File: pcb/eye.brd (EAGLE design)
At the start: 158.8 x 54 mm, 92 parts, among them J2 JST-ZH-5SMD-RA, U1 WS2812, U10 WS2812, U11 WS2812, U12 WS2812, U13 WS2812, U14 WS2812, U15 WS2812, U16 WS2812, U17 WS2812, U18 WS2812, U19 WS2812, U2 WS2812, U20 WS2812, U21 WS2812, U22 WS2812, U23 WS2812, U24 WS2812, U25 WS2812, U26 WS2812, U27 WS2812, U28 WS2812, U29 WS2812, U3 WS2812, U30 WS2812, U31 WS2812, U32 WS2812, U33 WS2812, U34 WS2812, U35 WS2812, U36 WS2812, U37 WS2812, U38 WS2812, U39 WS2812, U4 WS2812, U40 WS2812, U41 WS2812, U42 WS2812, U43 WS2812, U44 WS2812, U45 WS2812, U46 WS2812, U47 WS2812, U48 WS2812, U49 WS2812, U5 WS2812, U50 WS2812, U51 WS2812, U52 WS2812, U53 WS2812, U54 WS2812, U55 WS2812, U56 WS2812, U57 WS2812, U58 WS2812, U59 WS2812, U6 WS2812, U60 WS2812, U61 32U4, U7 WS2812, U8 WS2812, U9 WS2812, X1 ECS-160-20-3X-TR

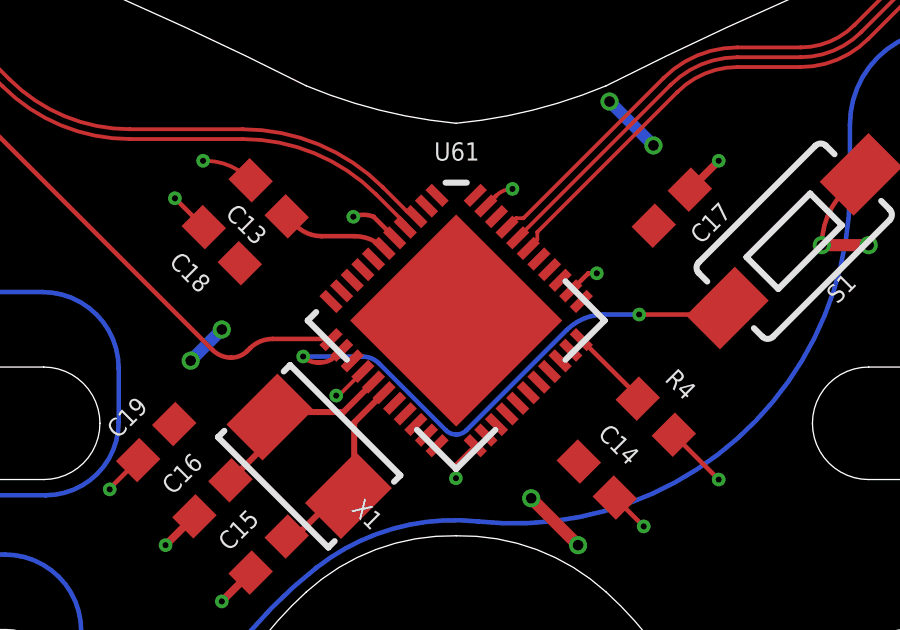
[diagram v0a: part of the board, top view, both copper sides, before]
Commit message: connect MCU grounds under EP
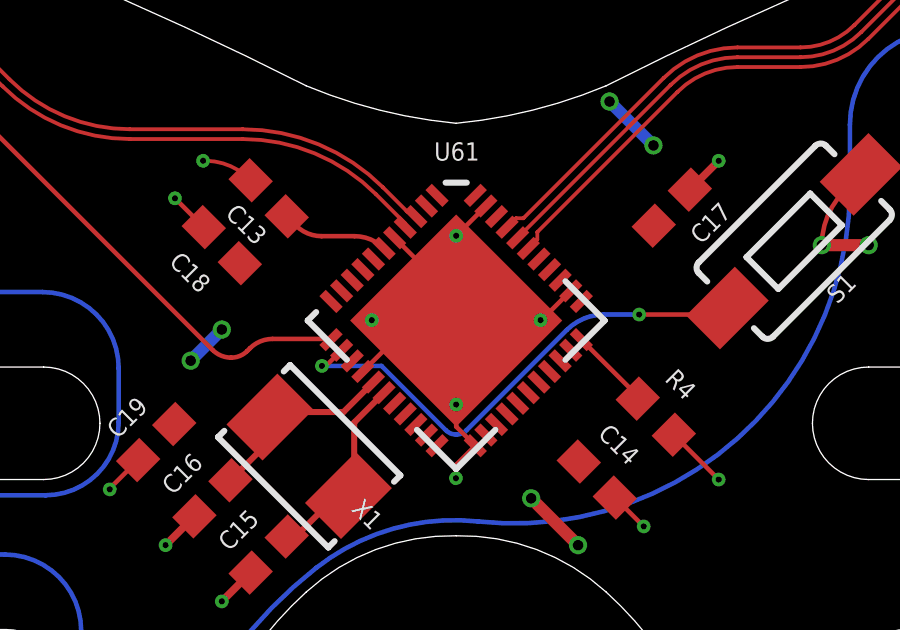
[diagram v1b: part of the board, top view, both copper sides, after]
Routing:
- net GND: track 223.1 -> 227.4 mm
- net RST: track 18.1 -> 17.1 mm
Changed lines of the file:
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@@
 <wire x1="10.5" y1="49.7" x2="10.1" y2="49.7" width="0.1524" layer="41"/>
 <wire x1="10.1" y1="49.7" x2="10.1" y2="50.9" width="0.1524" layer="41"/>
-<wire x1="76.2" y1="42.8" x2="80" y2="39" width="0.1524" layer="41"/>
-<wire x1="80" y1="39" x2="83.8" y2="42.8" width="0.1524" layer="41"/>
-<wire x1="83.8" y1="42.8" x2="80" y2="46.6" width="0.1524" layer="41"/>
-<wire x1="80" y1="46.6" x2="76.2" y2="42.8" width="0.1524" layer="41"/>
+<wire x1="77.6" y1="41.3" x2="80" y2="38.9" width="0.1524" layer="41"/>
+<wire x1="80.3" y1="39.3" x2="83.8" y2="42.8" width="0.1524" layer="41"/>
+<wire x1="83.8" y1="42.8" x2="83.5" y2="43.1" width="0.1524" layer="41"/>
+<wire x1="83.2" y1="43.5" x2="80.7" y2="46" width="0.1524" layer="41"/>
+<wire x1="80.3" y1="46.3" x2="80" y2="46.6" width="0.1524" layer="41"/>
+<wire x1="80" y1="46.6" x2="78.7" y2="45.3" width="0.1524" layer="41"/>
+<wire x1="78.2" y1="44.8" x2="76.2" y2="42.8" width="0.1524" layer="41"/>
+<wire x1="76.2" y1="42.8" x2="76.2" y2="42.7" width="0.1524" layer="41"/>
+<wire x1="76.2" y1="42.7" x2="77.2" y2="41.7" width="0.1524" layer="41"/>
 </plain>
 <attributes>
@@
 <wire x1="73.14895625" y1="34.39895625" x2="72.1875" y2="33.4375" width="0.254" layer="1"/>
 <via x="72.1875" y="33.4375" extent="1-16" drill="0.2"/>
-<wire x1="77.9493875" y1="45.557715625" x2="77.248340625" y2="46.2587625" width="0.1524" layer="1"/>
-<wire x1="77.248340625" y1="46.2587625" x2="76.5712625" y2="46.2587625" width="0.1524" layer="1" curve="45"/>
-<via x="76.5712625" y="46.2587625" extent="1-16" drill="0.2"/>
 <wire x1="73.14895625" y1="47.476040625" x2="71.682228125" y2="48.125" width="0.127" layer="1" curve="45"/>
 <wire x1="71.682228125" y1="48.125" x2="71.5625" y2="48.125" width="0.127" layer="1"/>
 <via x="71.5625" y="48.125" extent="1-16" drill="0.2"/>
-<wire x1="80.989946875" y1="46.618375" x2="81.335684375" y2="46.9641125" width="0.1524" layer="1"/>
-<wire x1="81.335684375" y1="46.9641125" x2="81.875" y2="47.1875" width="0.127" layer="1" curve="-45"/>
-<via x="81.875" y="47.1875" extent="1-16" drill="0.2"/>
-<wire x1="84.6875" y1="44.375" x2="84.403428125" y2="44.375" width="0.1524" layer="1"/>
-<wire x1="84.403428125" y1="44.375" x2="83.818375" y2="43.789946875" width="0.1524" layer="1"/>
-<via x="84.6875" y="44.375" extent="1-16" drill="0.2"/>
-<wire x1="76.888728125" y1="41.102940625" x2="76.042775" y2="40.2569875" width="0.127" layer="1"/>
-<wire x1="76.00138125" y1="40.29838125" x2="76.042775" y2="40.2569875" width="0.127" layer="1"/>
-<via x="76.00138125" y="40.29838125" extent="1-16" drill="0.2"/>
 <via x="88.75" y="48.125" extent="1-16" drill="0.2"/>
 <wire x1="141.15" y1="54.2" x2="141.947896875" y2="54.2" width="0.1524" layer="1"/>
@@
 <wire x1="93.4948" y1="47.671578125" x2="92.93121875" y2="47.107996875" width="0.1524" layer="1"/>
 <wire x1="92.93121875" y1="47.107996875" x2="92.1875" y2="45.3125" width="0.1524" layer="1" curve="45"/>
+<via x="80" y="45.625" extent="1-16" drill="0.2"/>
+<via x="82.8125" y="42.8125" extent="1-16" drill="0.2"/>
+<via x="77.1875" y="42.8125" extent="1-16" drill="0.2"/>
+<via x="80" y="40" extent="1-16" drill="0.2"/>
+<wire x1="76.888728125" y1="41.102940625" x2="77.6607875" y2="41.875" width="0.1524" layer="1"/>
+<wire x1="80.63639375" y1="38.62806875" x2="80" y2="39.2644625" width="0.1524" layer="1"/>
+<wire x1="80" y1="39.2644625" x2="80" y2="40" width="0.1524" layer="1"/>
+<wire x1="77.9493875" y1="45.557715625" x2="78.75" y2="44.757103125" width="0.1524" layer="1"/>
+<wire x1="80.989946875" y1="46.618375" x2="80.989946875" y2="46.614946875" width="0.1524" layer="1"/>
+<wire x1="80.989946875" y1="46.614946875" x2="80" y2="45.625" width="0.1524" layer="1"/>
+<wire x1="83.818375" y1="43.789946875" x2="82.840928125" y2="42.8125" width="0.1524" layer="1"/>
+<wire x1="82.840928125" y1="42.8125" x2="82.8125" y2="42.8125" width="0.1524" layer="1"/>
+<wire x1="77.1875" y1="42.8125" x2="77.6607875" y2="42.3392125" width="0.1524" layer="1"/>
+<wire x1="77.6607875" y1="42.3392125" x2="77.6607875" y2="41.875" width="0.1524" layer="1"/>
+<wire x1="78.75" y1="44.757103125" x2="79.132103125" y2="44.757103125" width="0.1524" layer="1"/>
+<wire x1="79.132103125" y1="44.757103125" x2="80" y2="45.625" width="0.1524" layer="1"/>
 </signal>
 <signal name="N$6">
@@
 <contactref element="U61" pad="13"/>
 <contactref element="S1" pad="2"/>
-<via x="74.9" y="41.6" extent="1-16" drill="0.2"/>
-<wire x1="74.9" y1="41.6" x2="76.872159375" y2="41.6" width="0.1524" layer="16"/>
-<wire x1="76.872159375" y1="41.6" x2="77.43181875" y2="41.36818125" width="0.1524" layer="16" curve="-45"/>
+<via x="75.525" y="41.2875" extent="1-16" drill="0.2"/>
+<wire x1="75.525" y1="41.2875" x2="77.5125" y2="41.2875" width="0.1524" layer="16"/>
 <wire x1="79.658578125" y1="39.141421875" x2="80" y2="39" width="0.1524" layer="16" curve="45"/>
 <wire x1="80" y1="39" x2="80.341421875" y2="39.141421875" width="0.1524" layer="16" curve="45"/>
@@
 <wire x1="86.1" y1="43" x2="88.278428125" y2="43" width="0.1524" layer="1"/>
 <wire x1="88.278428125" y1="43" x2="89.040028125" y2="43.21680625" width="0.1524" layer="1" curve="45"/>
-<wire x1="77.43181875" y1="41.36818125" x2="79.658578125" y2="39.141421875" width="0.1524" layer="16"/>
+<wire x1="77.5125" y1="41.2875" x2="79.658578125" y2="39.141421875" width="0.1524" layer="16"/>
 <wire x1="80.341421875" y1="39.141421875" x2="83.685340625" y2="42.485340625" width="0.1524" layer="16"/>
 <wire x1="76.181621875" y1="41.81005" x2="75.992890625" y2="41.62131875" width="0.1524" layer="1"/>
-<wire x1="75.992890625" y1="41.62131875" x2="75.458578125" y2="41.4" width="0.1524" layer="1" curve="-45"/>
-<wire x1="75.458578125" y1="41.4" x2="75.38284375" y2="41.4" width="0.1524" layer="1"/>
-<wire x1="75.38284375" y1="41.4" x2="74.9" y2="41.6" width="0.1524" layer="1" curve="-45"/>
+<wire x1="76.181621875" y1="41.81005" x2="75.659071875" y2="41.2875" width="0.1524" layer="1"/>
+<wire x1="75.659071875" y1="41.2875" x2="75.525" y2="41.2875" width="0.1524" layer="1"/>
 </signal>
 <signal name="N$77">

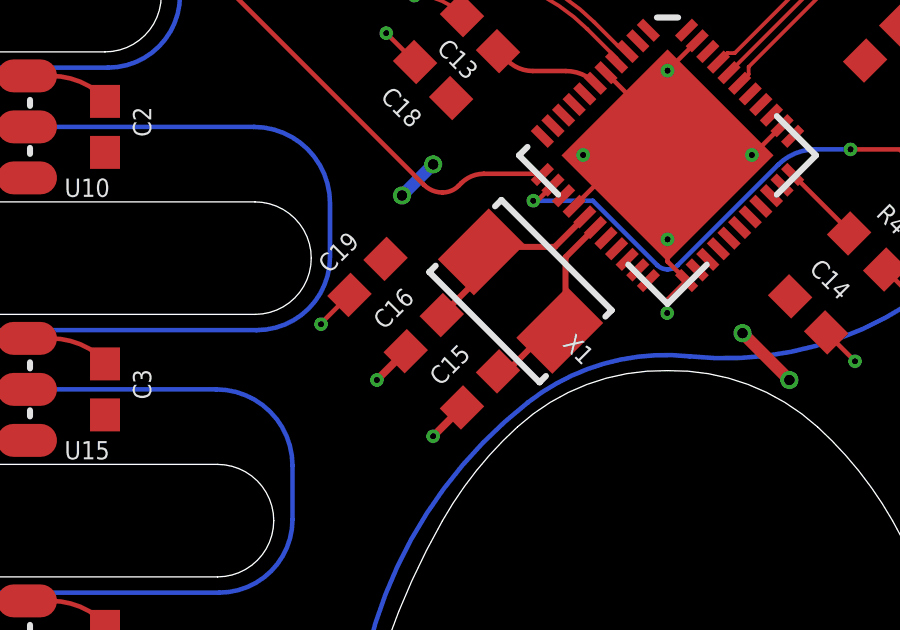
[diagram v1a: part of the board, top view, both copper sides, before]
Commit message: fix X1 silkscreen and caps
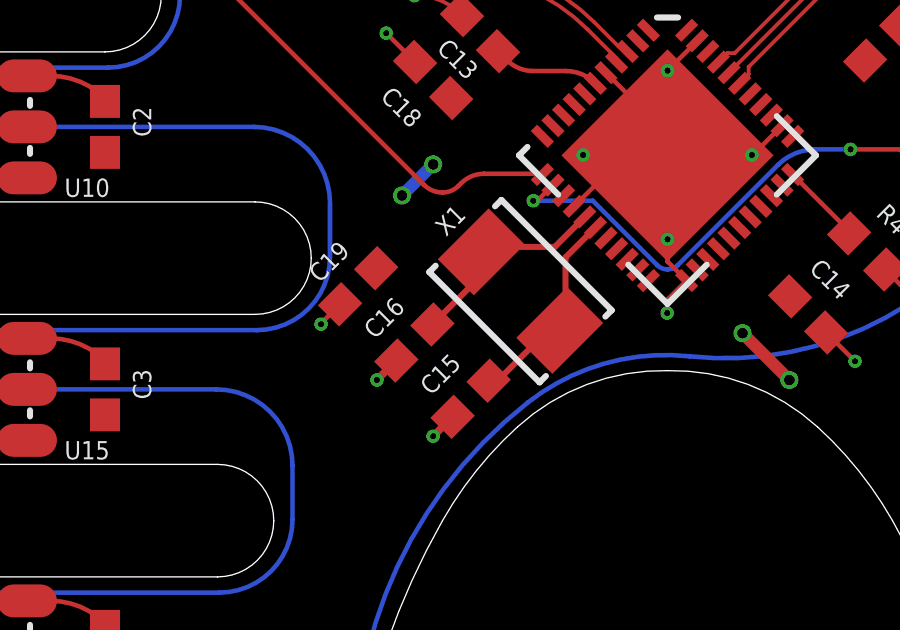
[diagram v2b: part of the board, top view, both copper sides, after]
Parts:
- moved C15 0.44 mm to (73.4, 34.7)
- moved C16 0.44 mm to (71.6, 36.6)
- moved C19 0.44 mm to (69.7, 38.4)
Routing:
- net GND: track 227.4 -> 226.1 mm
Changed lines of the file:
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@@
 <setting verticaltext="up"/>
 </settings>
-<grid distance="0.1" unitdist="mm" unit="mm" style="lines" multiple="1" display="yes" altdistance="5" altunitdist="mil" altunit="mil"/>
+<grid distance="0.3125" unitdist="mm" unit="mm" style="lines" multiple="1" display="yes" altdistance="5" altunitdist="mil" altunit="mil"/>
 <layers>
 <layer number="1" name="Top" color="4" fill="1" visible="yes" active="yes"/>
@@
 </element>
 <element name="X1" library="SparkFun-Clocks" package="CRYSTAL-SMD-5X3.2-2PAD" value="ECS-160-20-3X-TR" x="75.1" y="38.275" smashed="yes" rot="R315">
-<attribute name="NAME" x="76.47204375" y="36.479271875" size="0.6096" layer="25" ratio="10" rot="R315"/>
+<attribute name="NAME" x="72.620728125" y="40.07204375" size="0.6096" layer="25" ratio="10" rot="R45"/>
 <attribute name="VALUE" x="68.095403125" y="39.35263125" size="1.27" layer="27" ratio="10" rot="R315"/>
 </element>
-<element name="C15" library="rcl" library_urn="urn:adsk.eagle:library:334" package="C0603" package3d_urn="urn:adsk.eagle:package:23616/2" value="20p" x="73.75" y="35" smashed="yes" rot="R225">
-<attribute name="NAME" x="73.046046875" y="36.562496875" size="0.6096" layer="25" rot="R225"/>
-<attribute name="POPULARITY" value="73" x="75.959703125" y="78.75223125" size="1.778" layer="27" font="vector" rot="R225" display="off"/>
-<attribute name="SPICEPREFIX" value="C" x="75.959703125" y="78.75223125" size="1.778" layer="27" font="vector" rot="R225" display="off"/>
-<attribute name="VALUE" x="72.851971875" y="37.694071875" size="1.27" layer="27" rot="R225"/>
-</element>
-<element name="C16" library="rcl" library_urn="urn:adsk.eagle:library:334" package="C0603" package3d_urn="urn:adsk.eagle:package:23616/2" value="20p" x="71.875" y="36.875" smashed="yes" rot="R225">
-<attribute name="NAME" x="71.171053125" y="38.437496875" size="0.6096" layer="25" rot="R225"/>
-<attribute name="POPULARITY" value="73" x="73.200828125" y="88.582178125" size="1.778" layer="27" font="vector" rot="R225" display="off"/>
-<attribute name="SPICEPREFIX" value="C" x="73.200828125" y="88.582178125" size="1.778" layer="27" font="vector" rot="R225" display="off"/>
-<attribute name="VALUE" x="70.976971875" y="39.569071875" size="1.27" layer="27" rot="R225"/>
+<element name="C15" library="rcl" library_urn="urn:adsk.eagle:library:334" package="C0603" package3d_urn="urn:adsk.eagle:package:23616/2" value="20p" x="73.4375" y="34.6875" smashed="yes" rot="R225">
+<attribute name="NAME" x="72.733546875" y="36.249996875" size="0.6096" layer="25" rot="R225"/>
+<attribute name="POPULARITY" value="73" x="75.647203125" y="78.43973125" size="1.778" layer="27" font="vector" rot="R225" display="off"/>
+<attribute name="SPICEPREFIX" value="C" x="75.647203125" y="78.43973125" size="1.778" layer="27" font="vector" rot="R225" display="off"/>
+<attribute name="VALUE" x="72.539471875" y="37.381571875" size="1.27" layer="27" rot="R225"/>
+</element>
+<element name="C16" library="rcl" library_urn="urn:adsk.eagle:library:334" package="C0603" package3d_urn="urn:adsk.eagle:package:23616/2" value="20p" x="71.5625" y="36.5625" smashed="yes" rot="R225">
+<attribute name="NAME" x="70.858553125" y="38.124996875" size="0.6096" layer="25" rot="R225"/>
+<attribute name="POPULARITY" value="73" x="72.888328125" y="88.269678125" size="1.778" layer="27" font="vector" rot="R225" display="off"/>
+<attribute name="SPICEPREFIX" value="C" x="72.888328125" y="88.269678125" size="1.778" layer="27" font="vector" rot="R225" display="off"/>
+<attribute name="VALUE" x="70.664471875" y="39.256571875" size="1.27" layer="27" rot="R225"/>
 </element>
 <element name="U61" library="SparkFun-IC-Microcontroller" package="QFN-44" value="32U4" x="80" y="42.8" smashed="yes" rot="R315">
@@
 <attribute name="VALUE" x="73.983553125" y="46.210528125" size="1.27" layer="27" rot="R135"/>
 </element>
-<element name="C19" library="rcl" library_urn="urn:adsk.eagle:library:334" package="C0603" package3d_urn="urn:adsk.eagle:package:23616/2" value="" x="70" y="38.75" smashed="yes" rot="R225">
-<attribute name="NAME" x="69.335525" y="40.3125" size="0.6096" layer="25" rot="R225"/>
-<attribute name="POPULARITY" value="73" x="70" y="38.75" size="1.778" layer="27" rot="R225" display="off"/>
-<attribute name="SPICEPREFIX" value="C" x="70" y="38.75" size="1.778" layer="27" rot="R225" display="off"/>
-<attribute name="VALUE" x="69.101975" y="40.546053125" size="1.27" layer="27" rot="R225"/>
+<element name="C19" library="rcl" library_urn="urn:adsk.eagle:library:334" package="C0603" package3d_urn="urn:adsk.eagle:package:23616/2" value="" x="69.6875" y="38.4375" smashed="yes" rot="R225">
+<attribute name="NAME" x="69.023025" y="40" size="0.6096" layer="25" rot="R225"/>
+<attribute name="POPULARITY" value="73" x="69.6875" y="38.4375" size="1.778" layer="27" rot="R225" display="off"/>
+<attribute name="SPICEPREFIX" value="C" x="69.6875" y="38.4375" size="1.778" layer="27" rot="R225" display="off"/>
+<attribute name="VALUE" x="68.789475" y="40.233553125" size="1.27" layer="27" rot="R225"/>
 </element>
 <element name="S1" library="SparkFun-Switches" package="TACTILE_SWITCH_SMD_6.0X3.5MM" value="MOMENTARY-SWITCH-SPST-SMD-6.0X3.5MM" x="91.267415625" y="45.44419375" smashed="yes" rot="R225">
@@
 <wire x1="7.45" y1="44.95" x2="7.5" y2="45" width="0.4064" layer="1" curve="90"/>
 <via x="7.5" y="45" extent="1-16" drill="0.35"/>
-<wire x1="71.27395625" y1="36.27395625" x2="70.3125" y2="35.3125" width="0.254" layer="1"/>
+<wire x1="70.96145625" y1="35.96145625" x2="70.3125" y2="35.3125" width="0.254" layer="1"/>
 <via x="70.3125" y="35.3125" extent="1-16" drill="0.2"/>
-<wire x1="73.14895625" y1="34.39895625" x2="72.1875" y2="33.4375" width="0.254" layer="1"/>
+<wire x1="72.83645625" y1="34.08645625" x2="72.1875" y2="33.4375" width="0.254" layer="1"/>
 <via x="72.1875" y="33.4375" extent="1-16" drill="0.2"/>
 <wire x1="73.14895625" y1="47.476040625" x2="71.682228125" y2="48.125" width="0.127" layer="1" curve="45"/>
@@
 <contactref element="C19" pad="2"/>
 <contactref element="C18" pad="2"/>
-<wire x1="69.39895625" y1="38.14895625" x2="68.471103125" y2="37.221103125" width="0.1524" layer="1"/>
+<wire x1="69.08645625" y1="37.83645625" x2="68.471103125" y2="37.221103125" width="0.1524" layer="1"/>
 <wire x1="68.471103125" y1="37.221103125" x2="68.450678125" y2="37.17179375" width="0.1524" layer="1" curve="45"/>
 <via x="68.450678125" y="37.17179375" extent="1-16" drill="0.2"/>
@@
 <wire x1="76.24289375" y1="39.75" x2="73.958703125" y2="39.75" width="0.2032" layer="1"/>
 <wire x1="73.79185" y1="39.583146875" x2="73.79185" y2="38.79185" width="0.3048" layer="1"/>
-<wire x1="73.79185" y1="38.79185" x2="72.476040625" y2="37.476040625" width="0.2032" layer="1"/>
+<wire x1="73.79185" y1="38.79185" x2="72.163540625" y2="37.163540625" width="0.2032" layer="1"/>
 </signal>
 <signal name="N$68">
@@
 <wire x1="76.6" y1="39.4" x2="76.6" y2="37.158703125" width="0.2032" layer="1"/>
 <wire x1="76.408146875" y1="36.96685" x2="76.01685" y2="36.96685" width="0.2032" layer="1"/>
-<wire x1="76.01685" y1="36.96685" x2="74.651040625" y2="35.601040625" width="0.2032" layer="1"/>
-<wire x1="74.651040625" y1="35.601040625" x2="74.351040625" y2="35.601040625" width="0.2032" layer="1"/>
+<wire x1="76.01685" y1="36.96685" x2="74.338540625" y2="35.288540625" width="0.2032" layer="1"/>
+<wire x1="74.338540625" y1="35.288540625" x2="74.038540625" y2="35.288540625" width="0.2032" layer="1"/>
 </signal>
 <signal name="RST">

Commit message: fix font
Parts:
- moved C17 0.88 mm to (86.6, 45.9)
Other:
- board text added: "DFU Bootloader"

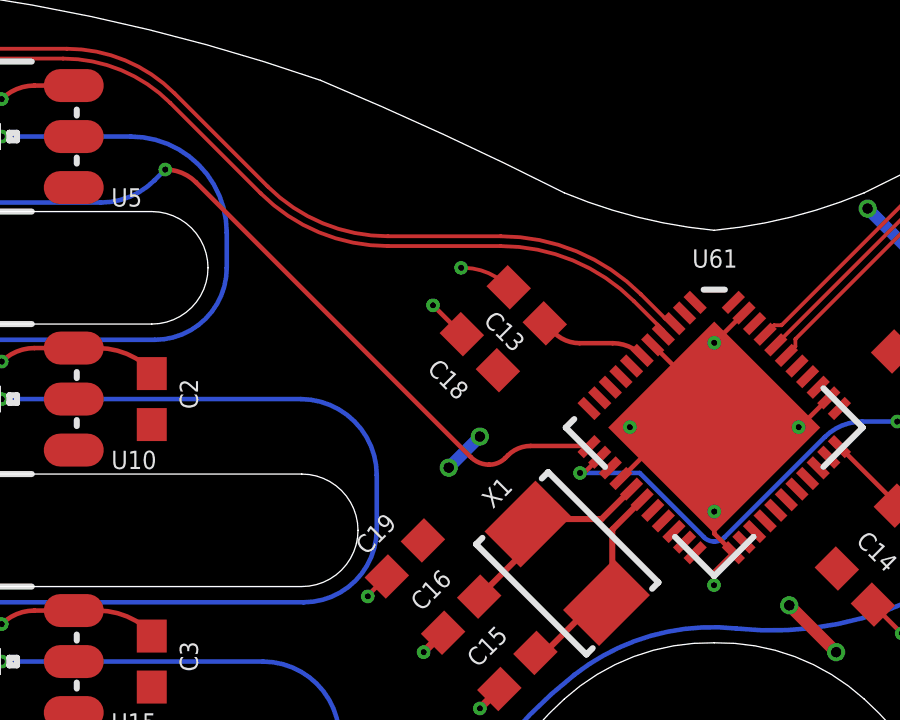
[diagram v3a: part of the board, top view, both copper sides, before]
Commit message: add 10uF VBUS cap
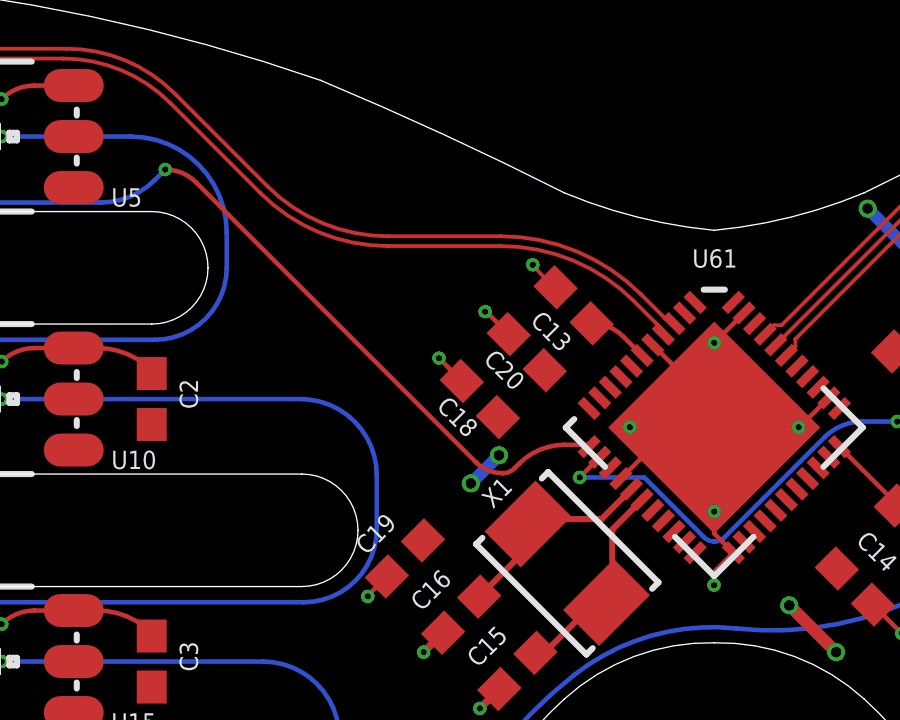
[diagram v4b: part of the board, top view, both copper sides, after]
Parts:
- added C20: 10u, rcl:C0603
- moved C13 1.56 mm to (75.3, 46.9)
- moved C18 1.56 mm to (72.2, 43.8)
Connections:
- net +5V: now also C20.1
- net GND: now also C20.2
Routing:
- net N$62: track 3.52 -> 2.13 mm
- net GND: track 226.1 -> 226.3 mm, vias 82 -> 83
